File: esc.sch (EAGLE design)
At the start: 35 parts, among them U1 AON6558, U2 AON6558, U3 AON6558, U4 AON6558, U5 ATTINY20, U6 DRV8701

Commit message: Update to V2.1
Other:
- moved on the sheet: U$2

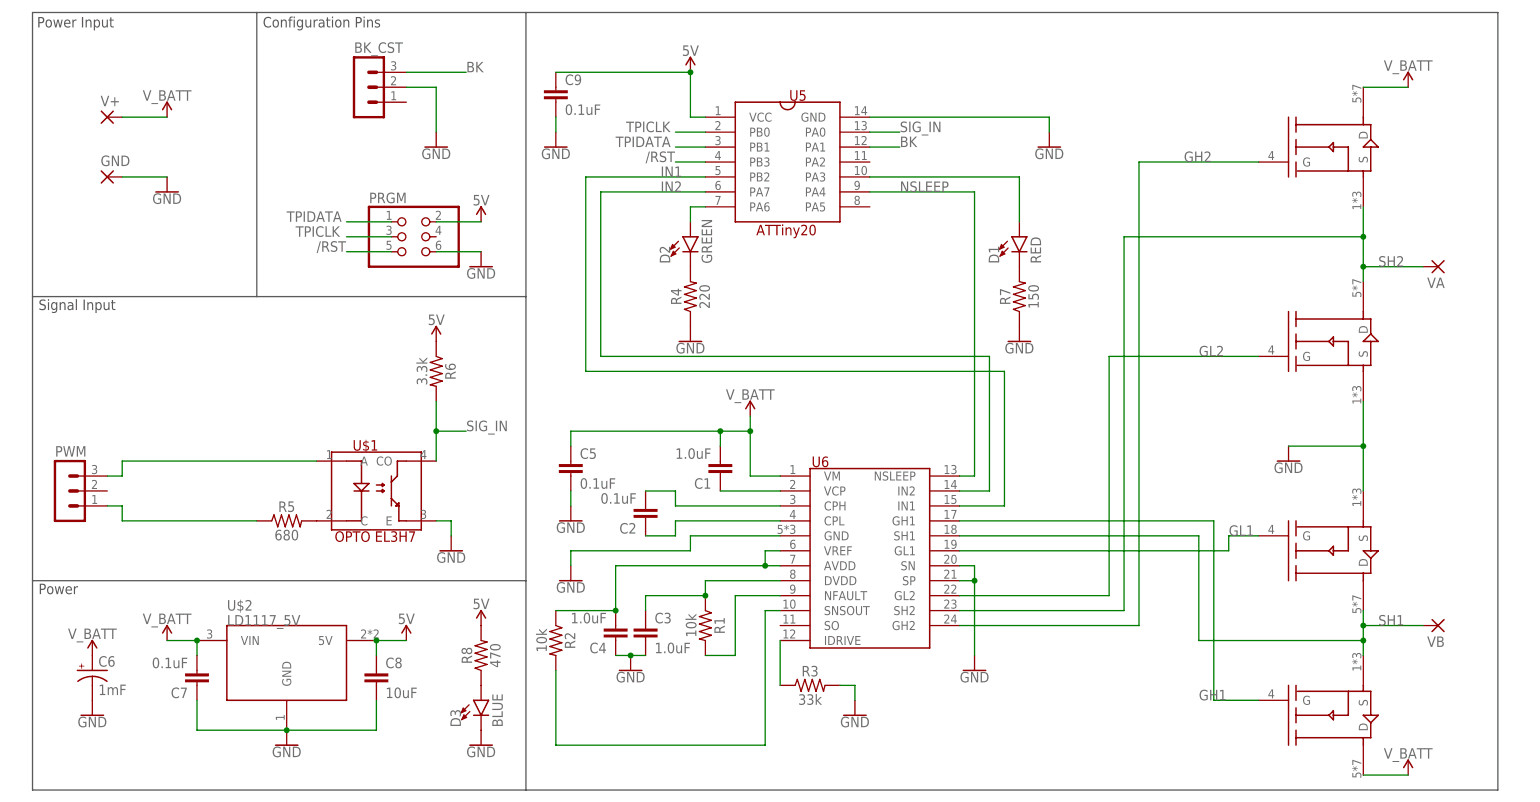
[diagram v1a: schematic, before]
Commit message: Update to board v3
New power connectors and compactify layout
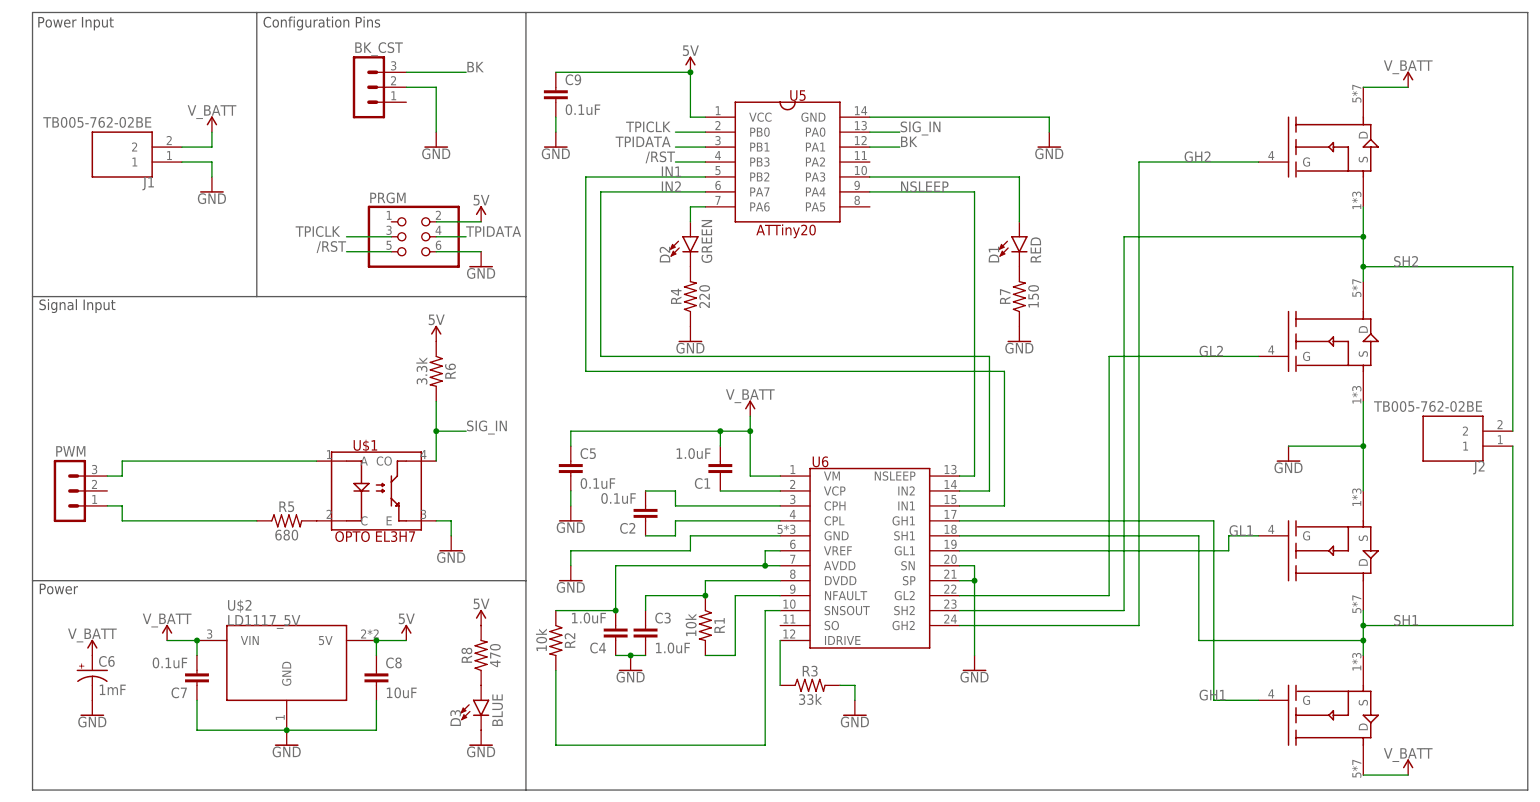
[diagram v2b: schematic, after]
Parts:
- removed GND, V+, VA, VB: (no value), wirepad:SMD5
- added J1, J2: TB005-762-02BE, TB005-762-02BE:TB005-762-02BE
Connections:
- net GND: now also J1.1; no longer GND.P
- net SH1: now also J2.1; no longer VB.P
- net SH2: now also J2.2; no longer VA.P
- net TPIDATA: now also PRGM.4; no longer PRGM.1
- net V_BATT: now also J1.2; no longer V+.P
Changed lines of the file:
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@@
 <?xml version="1.0" encoding="utf-8"?>
 <!DOCTYPE eagle SYSTEM "eagle.dtd">
-<eagle version="9.3.0">
+<eagle version="9.4.2">
 <drawing>
 <settings>
@@
 <part name="SUPPLY10" library="SparkFun-PowerSymbols" deviceset="5V" device=""/>
 <part name="GND6" library="SparkFun-PowerSymbols" deviceset="GND" device=""/>
-<part name="GND" library="wirepad" library_urn="urn:adsk.eagle:library:412" deviceset="SMD5" device="" package3d_urn="urn:adsk.eagle:package:30841/1"/>
-<part name="V+" library="wirepad" library_urn="urn:adsk.eagle:library:412" deviceset="SMD5" device="" package3d_urn="urn:adsk.eagle:package:30841/1"/>
 <part name="GND13" library="SparkFun-PowerSymbols" deviceset="GND" device=""/>
 <part name="SUPPLY11" library="SparkFun-PowerSymbols" deviceset="V_BATT" device=""/>
 <part name="BK_CST" library="con-lstb" library_urn="urn:adsk.eagle:library:162" deviceset="MA03-1" device="" package3d_urn="urn:adsk.eagle:package:8339/1"/>
 <part name="GND14" library="SparkFun-PowerSymbols" deviceset="GND" device=""/>
-<part name="VA" library="wirepad" library_urn="urn:adsk.eagle:library:412" deviceset="SMD5" device="" package3d_urn="urn:adsk.eagle:package:30841/1"/>
-<part name="VB" library="wirepad" library_urn="urn:adsk.eagle:library:412" deviceset="SMD5" device="" package3d_urn="urn:adsk.eagle:package:30841/1"/>
 <part name="GND15" library="SparkFun-PowerSymbols" deviceset="GND" device=""/>
 <part name="C9" library="SparkFun-Capacitors" deviceset="0.1UF" device="-0603-25V-5%" value="0.1uF"/>
@@
 <part name="GND17" library="SparkFun-PowerSymbols" deviceset="GND" device=""/>
 <part name="C8" library="SparkFun-Capacitors" deviceset="10UF" device="-0603-6.3V-20%" value="10uF"/>
+<part name="J1" library="TB005-762-02BE" deviceset="TB005-762-02BE" device=""/>
+<part name="J2" library="TB005-762-02BE" deviceset="TB005-762-02BE" device=""/>
 </parts>
 <sheets>
@@
 <text x="-146.558" y="63.5" size="1.778" layer="97">Power Input</text>
 <text x="-146.304" y="15.494" size="1.778" layer="97">Signal Input</text>
-<wire x1="-63.5" y1="-66.04" x2="101.6" y2="-66.04" width="0.1524" layer="97"/>
-<wire x1="101.6" y1="66.04" x2="-63.5" y2="66.04" width="0.1524" layer="97"/>
-<wire x1="101.6" y1="-66.04" x2="101.6" y2="66.04" width="0.1524" layer="97"/>
+<wire x1="-63.5" y1="-66.04" x2="106.68" y2="-66.04" width="0.1524" layer="97"/>
+<wire x1="106.68" y1="66.04" x2="-63.5" y2="66.04" width="0.1524" layer="97"/>
+<wire x1="106.68" y1="-66.04" x2="106.68" y2="66.04" width="0.1524" layer="97"/>
 </plain>
 <instances>
@@
 <attribute name="VALUE" x="-71.12" y="22.606" size="1.778" layer="96" align="top-center"/>
 </instance>
-<instance part="GND" gate="1" x="-134.62" y="38.1" smashed="yes">
-<attribute name="NAME" x="-135.763" y="39.9542" size="1.778" layer="95"/>
-<attribute name="VALUE" x="-135.763" y="34.798" size="1.778" layer="96"/>
-</instance>
-<instance part="V+" gate="1" x="-134.62" y="48.26" smashed="yes">
-<attribute name="NAME" x="-135.763" y="50.1142" size="1.778" layer="95"/>
-<attribute name="VALUE" x="-135.763" y="44.958" size="1.778" layer="96"/>
-</instance>
-<instance part="GND13" gate="1" x="-124.46" y="35.56" smashed="yes">
-<attribute name="VALUE" x="-124.46" y="35.306" size="1.778" layer="96" align="top-center"/>
-</instance>
-<instance part="SUPPLY11" gate="G$1" x="-124.46" y="48.26" smashed="yes">
-<attribute name="VALUE" x="-124.46" y="51.054" size="1.778" layer="96" align="bottom-center"/>
+<instance part="GND13" gate="1" x="-116.84" y="35.56" smashed="yes">
+<attribute name="VALUE" x="-116.84" y="35.306" size="1.778" layer="96" align="top-center"/>
+</instance>
+<instance part="SUPPLY11" gate="G$1" x="-116.84" y="45.72" smashed="yes">
+<attribute name="VALUE" x="-116.84" y="48.514" size="1.778" layer="96" align="bottom-center"/>
 </instance>
 <instance part="BK_CST" gate="G$1" x="-91.44" y="53.34" smashed="yes">
@@
 <attribute name="VALUE" x="-78.74" y="42.926" size="1.778" layer="96" align="top-center"/>
 </instance>
-<instance part="VA" gate="1" x="91.44" y="22.86" smashed="yes" rot="R180">
-<attribute name="NAME" x="92.583" y="21.0058" size="1.778" layer="95" rot="R180"/>
-<attribute name="VALUE" x="92.583" y="26.162" size="1.778" layer="96" rot="R180"/>
-</instance>
-<instance part="VB" gate="1" x="91.44" y="-38.1" smashed="yes" rot="R180">
-<attribute name="NAME" x="92.583" y="-39.9542" size="1.778" layer="95" rot="R180"/>
-<attribute name="VALUE" x="92.583" y="-34.798" size="1.778" layer="96" rot="R180"/>
-</instance>
 <instance part="GND15" gate="1" x="66.04" y="-10.16" smashed="yes">
 <attribute name="VALUE" x="66.04" y="-10.414" size="1.778" layer="96" align="top-center"/>
@@
 <attribute name="NAME" x="-87.376" y="-45.339" size="1.778" layer="95" font="vector"/>
 <attribute name="VALUE" x="-87.376" y="-50.419" size="1.778" layer="96" font="vector"/>
+</instance>
+<instance part="J1" gate="G$1" x="-132.08" y="43.18" smashed="yes" rot="R180">
+<attribute name="NAME" x="-126.5" y="38.1" size="1.778" layer="95" rot="R180"/>
+<attribute name="VALUE" x="-127" y="48.26" size="1.778" layer="96" rot="R180"/>
+</instance>
+<instance part="J2" gate="G$1" x="93.98" y="-5.08" smashed="yes" rot="R180">
+<attribute name="NAME" x="99.56" y="-10.16" size="1.778" layer="95" rot="R180"/>
+<attribute name="VALUE" x="99.06" y="0" size="1.778" layer="96" rot="R180"/>
 </instance>
 </instances>
@@
 </segment>
 <segment>
-<pinref part="V+" gate="1" pin="P"/>
-<wire x1="-132.08" y1="48.26" x2="-124.46" y2="48.26" width="0.1524" layer="91"/>
+<pinref part="J1" gate="G$1" pin="2"/>
 <pinref part="SUPPLY11" gate="G$1" pin="V_BATT"/>
+<wire x1="-121.92" y1="43.18" x2="-116.84" y2="43.18" width="0.1524" layer="91"/>
+<wire x1="-116.84" y1="43.18" x2="-116.84" y2="45.72" width="0.1524" layer="91"/>
 </segment>
 </net>
@@
 </segment>
 <segment>
-<pinref part="GND" gate="1" pin="P"/>
-<wire x1="-132.08" y1="38.1" x2="-124.46" y2="38.1" width="0.1524" layer="91"/>
-<pinref part="GND13" gate="1" pin="GND"/>
-</segment>
-<segment>
 <pinref part="BK_CST" gate="G$1" pin="2"/>
 <pinref part="GND14" gate="1" pin="GND"/>
@@
 <pinref part="GND17" gate="1" pin="GND"/>
 </segment>
+<segment>
+<pinref part="J1" gate="G$1" pin="1"/>
+<pinref part="GND13" gate="1" pin="GND"/>
+<wire x1="-121.92" y1="40.64" x2="-116.84" y2="40.64" width="0.1524" layer="91"/>
+<wire x1="-116.84" y1="40.64" x2="-116.84" y2="38.1" width="0.1524" layer="91"/>
+</segment>
 </net>
 <net name="SH1" class="1">
@@
 <wire x1="50.8" y1="-22.86" x2="50.8" y2="-40.64" width="0.1524" layer="91"/>
 <pinref part="U4" gate="G$1" pin="S"/>
-<label x="81.28" y="-38.1" size="1.778" layer="95"/>
+<label x="83.82" y="-38.1" size="1.778" layer="95"/>
 <wire x1="78.74" y1="-43.18" x2="78.74" y2="-40.64" width="0.1524" layer="91"/>
 <pinref part="U3" gate="G$1" pin="D"/>
@@
 <wire x1="78.74" y1="-38.1" x2="78.74" y2="-35.56" width="0.1524" layer="91"/>
 <junction x="78.74" y="-38.1"/>
-<pinref part="VB" gate="1" pin="P"/>
-<wire x1="78.74" y1="-38.1" x2="88.9" y2="-38.1" width="0.1524" layer="91"/>
 <wire x1="50.8" y1="-40.64" x2="78.74" y2="-40.64" width="0.1524" layer="91"/>
 <junction x="78.74" y="-40.64"/>
+<pinref part="J2" gate="G$1" pin="1"/>
+<wire x1="78.74" y1="-38.1" x2="104.14" y2="-38.1" width="0.1524" layer="91"/>
+<wire x1="104.14" y1="-38.1" x2="104.14" y2="-7.62" width="0.1524" layer="91"/>
 </segment>
 </net>
@@
 <pinref part="U1" gate="G$1" pin="S"/>
 <pinref part="U2" gate="G$1" pin="D"/>
-<label x="81.28" y="22.86" size="1.778" layer="95"/>
+<label x="83.82" y="22.86" size="1.778" layer="95"/>
 <wire x1="78.74" y1="33.02" x2="78.74" y2="27.94" width="0.1524" layer="91"/>
 <wire x1="78.74" y1="27.94" x2="78.74" y2="22.86" width="0.1524" layer="91"/>
 <wire x1="78.74" y1="22.86" x2="78.74" y2="20.32" width="0.1524" layer="91"/>
-<wire x1="78.74" y1="22.86" x2="88.9" y2="22.86" width="0.1524" layer="91"/>
-<junction x="78.74" y="22.86"/>
-<pinref part="VA" gate="1" pin="P"/>
 <wire x1="38.1" y1="27.94" x2="78.74" y2="27.94" width="0.1524" layer="91"/>
 <junction x="78.74" y="27.94"/>
+<junction x="78.74" y="22.86"/>
+<pinref part="J2" gate="G$1" pin="2"/>
+<wire x1="78.74" y1="22.86" x2="104.14" y2="22.86" width="0.1524" layer="91"/>
+<wire x1="104.14" y1="22.86" x2="104.14" y2="-5.08" width="0.1524" layer="91"/>
 </segment>
 </net>
@@
 </segment>
 <segment>
-<pinref part="PRGM" gate="A" pin="1"/>
-<wire x1="-86.36" y1="30.48" x2="-93.98" y2="30.48" width="0.1524" layer="91"/>
-<label x="-104.14" y="30.48" size="1.778" layer="95"/>
-</segment>
-</net>
+<label x="-73.66" y="27.94" size="1.778" layer="95"/>
+<pinref part="PRGM" gate="A" pin="4"/>
+<wire x1="-73.66" y1="27.94" x2="-78.74" y2="27.94" width="0.1524" layer="91"/>
+</segment>
+</net>

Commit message: Add current sense features
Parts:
- added R9: 12m, rcl:R-US_R2512
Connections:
- net N$11 renamed SNSOUT
- removed net N$10: R1.2, U6.NFAULT
- new net N$14: R9.1, U2.S, U3.S, U6.SP
- new net NFAULT: R1.2, U5.PA5, U6.NFAULT
- new net SO: U5.PA2, U6.SO
- net GND: now also R9.2; no longer U2.S, U3.S, U6.SP
- net N$5: now also R2.1
- net N$7: no longer R2.1
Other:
- moved on the sheet: C3, C4, R1, R2
